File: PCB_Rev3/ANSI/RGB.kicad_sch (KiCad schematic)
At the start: 62 parts

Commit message: Wires optimization.
More GND hole still needed...
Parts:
- RGB1, RGB10, RGB11, RGB12, RGB13, RGB14, RGB15, RGB16, RGB17, RGB18, RGB19, RGB2, RGB20, RGB21, RGB22, RGB23, RGB24, RGB25, RGB26, RGB27, RGB28, RGB29, RGB3, RGB30, RGB31, RGB32, RGB33, RGB34, RGB35, RGB36, RGB37, RGB38, RGB39, RGB4, RGB40, RGB41, RGB42, RGB43, RGB44, RGB45, RGB46, RGB47, RGB48, RGB49, RGB5, RGB50, RGB51, RGB52, RGB53, RGB54, RGB55, RGB56, RGB57, RGB58, RGB59, RGB6, RGB60, RGB61, RGB62, RGB7, RGB8, RGB9: footprint RGB:ws2812B_6028 -> PH60:WS2812B_Reverse
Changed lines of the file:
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@@
 			)
 		)
-		(property "Footprint" "RGB:ws2812B_6028"
+		(property "Footprint" "PH60:WS2812B_Reverse"
 			(at 185.42 64.77 0)
 			(effects
@@
 			)
 		)
-		(property "Footprint" "RGB:ws2812B_6028"
+		(property "Footprint" "PH60:WS2812B_Reverse"
 			(at 43.18 85.09 0)
 			(effects
@@
 			)
 		)
-		(property "Footprint" "RGB:ws2812B_6028"
+		(property "Footprint" "PH60:WS2812B_Reverse"
 			(at 185.42 105.41 0)
 			(effects
@@
 			)
 		)
-		(property "Footprint" "RGB:ws2812B_6028"
+		(property "Footprint" "PH60:WS2812B_Reverse"
 			(at 398.78 105.41 0)
 			(effects
@@
 			)
 		)
-		(property "Footprint" "RGB:ws2812B_6028"
+		(property "Footprint" "PH60:WS2812B_Reverse"
 			(at 78.74 105.41 0)
 			(effects
@@
 			)
 		)
-		(property "Footprint" "RGB:ws2812B_6028"
+		(property "Footprint" "PH60:WS2812B_Reverse"
 			(at 363.22 105.41 0)
 			(effects
@@
 			)
 		)
-		(property "Footprint" "RGB:ws2812B_6028"
+		(property "Footprint" "PH60:WS2812B_Reverse"
 			(at 469.9 64.77 0)
 			(effects
@@
 			)
 		)
-		(property "Footprint" "RGB:ws2812B_6028"
+		(property "Footprint" "PH60:WS2812B_Reverse"
 			(at 185.42 125.73 0)
 			(effects
@@
 			)
 		)
-		(property "Footprint" "RGB:ws2812B_6028"
+		(property "Footprint" "PH60:WS2812B_Reverse"
 			(at 220.98 85.09 0)
 			(effects
@@
 			)
 		)
-		(property "Footprint" "RGB:ws2812B_6028"
+		(property "Footprint" "PH60:WS2812B_Reverse"
 			(at 43.18 125.73 0)
 			(effects
@@
 			)
 		)
-		(property "Footprint" "RGB:ws2812B_6028"
+		(property "Footprint" "PH60:WS2812B_Reverse"
 			(at 327.66 44.45 0)
 			(effects
@@
 			)
 		)
-		(property "Footprint" "RGB:ws2812B_6028"
+		(property "Footprint" "PH60:WS2812B_Reverse"
 			(at 434.34 44.45 0)
 			(effects
@@
 			)
 		)
-		(property "Footprint" "RGB:ws2812B_6028"
+		(property "Footprint" "PH60:WS2812B_Reverse"
 			(at 256.54 44.45 0)
 			(effects
@@
 			)
 		)
-		(property "Footprint" "RGB:ws2812B_6028"
+		(property "Footprint" "PH60:WS2812B_Reverse"
 			(at 505.46 44.45 0)
 			(effects
@@
 			)
 		)
-		(property "Footprint" "RGB:ws2812B_6028"
+		(property "Footprint" "PH60:WS2812B_Reverse"
 			(at 363.22 64.77 0)
 			(effects
@@
 			)
 		)
-		(property "Footprint" "RGB:ws2812B_6028"
+		(property "Footprint" "PH60:WS2812B_Reverse"
 			(at 185.42 44.45 0)
 			(effects
@@
 			)
 		)
-		(property "Footprint" "RGB:ws2812B_6028"
+		(property "Footprint" "PH60:WS2812B_Reverse"
 			(at 469.9 85.09 0)
 			(effects
@@
 			)
 		)
-		(property "Footprint" "RGB:ws2812B_6028"
+		(property "Footprint" "PH60:WS2812B_Reverse"
 			(at 256.54 64.77 0)
 			(effects
@@
 			)
 		)
-		(property "Footprint" "RGB:ws2812B_6028"
+		(property "Footprint" "PH60:WS2812B_Reverse"
 			(at 149.86 64.77 0)
 			(effects
@@
 			)
 		)
-		(property "Footprint" "RGB:ws2812B_6028"
+		(property "Footprint" "PH60:WS2812B_Reverse"
 			(at 434.34 64.77 0)
 			(effects
@@
 			)
 		)
-		(property "Footprint" "RGB:ws2812B_6028"
+		(property "Footprint" "PH60:WS2812B_Reverse"
 			(at 114.3 64.77 0)
 			(effects
@@
 			)
 		)
-		(property "Footprint" "RGB:ws2812B_6028"
+		(property "Footprint" "PH60:WS2812B_Reverse"
 			(at 292.1 44.45 0)
 			(effects
@@
 			)
 		)
-		(property "Footprint" "RGB:ws2812B_6028"
+		(property "Footprint" "PH60:WS2812B_Reverse"
 			(at 78.74 64.77 0)
 			(effects
@@
 			)
 		)
-		(property "Footprint" "RGB:ws2812B_6028"
+		(property "Footprint" "PH60:WS2812B_Reverse"
 			(at 43.18 105.41 0)
 			(effects
@@
 			)
 		)
-		(property "Footprint" "RGB:ws2812B_6028"
+		(property "Footprint" "PH60:WS2812B_Reverse"
 			(at 78.74 85.09 0)
 			(effects
@@
 			)
 		)
-		(property "Footprint" "RGB:ws2812B_6028"
+		(property "Footprint" "PH60:WS2812B_Reverse"
 			(at 43.18 64.77 0)
 			(effects
@@
 			)
 		)
-		(property "Footprint" "RGB:ws2812B_6028"
+		(property "Footprint" "PH60:WS2812B_Reverse"
 			(at 363.22 44.45 0)
 			(effects
@@
 			)
 		)
-		(property "Footprint" "RGB:ws2812B_6028"
+		(property "Footprint" "PH60:WS2812B_Reverse"
 			(at 220.98 44.45 0)
 			(effects
@@
 			)
 		)
-		(property "Footprint" "RGB:ws2812B_6028"
+		(property "Footprint" "PH60:WS2812B_Reverse"
 			(at 469.9 44.45 0)
 			(effects
@@
 			)
 		)
-		(property "Footprint" "RGB:ws2812B_6028"
+		(property "Footprint" "PH60:WS2812B_Reverse"
 			(at 292.1 85.09 0)
 			(effects
@@
 			)
 		)
-		(property "Footprint" "RGB:ws2812B_6028"
+		(property "Footprint" "PH60:WS2812B_Reverse"
 			(at 114.3 44.45 0)
 			(effects
@@
 			)
 		)
-		(property "Footprint" "RGB:ws2812B_6028"
+		(property "Footprint" "PH60:WS2812B_Reverse"
 			(at 78.74 125.73 0)
 			(effects
@@
 			)
 		)
-		(property "Footprint" "RGB:ws2812B_6028"
+		(property "Footprint" "PH60:WS2812B_Reverse"
 			(at 220.98 64.77 0)
 			(effects
@@
 			)
 		)
-		(property "Footprint" "RGB:ws2812B_6028"
+		(property "Footprint" "PH60:WS2812B_Reverse"
 			(at 398.78 44.45 0)
 			(effects
@@
 			)
 		)
-		(property "Footprint" "RGB:ws2812B_6028"
+		(property "Footprint" "PH60:WS2812B_Reverse"
 			(at 398.78 64.77 0)
 			(effects
@@
 			)
 		)
-		(property "Footprint" "RGB:ws2812B_6028"
+		(property "Footprint" "PH60:WS2812B_Reverse"
 			(at 114.3 105.41 0)
 			(effects
@@
 			)
 		)
-		(property "Footprint" "RGB:ws2812B_6028"
+		(property "Footprint" "PH60:WS2812B_Reverse"
 			(at 43.18 44.45 0)
 			(effects
@@
 			)
 		)
-		(property "Footprint" "RGB:ws2812B_6028"
+		(property "Footprint" "PH60:WS2812B_Reverse"
 			(at 505.46 64.77 0)
 			(effects
@@
 			)
 		)
-		(property "Footprint" "RGB:ws2812B_6028"
+		(property "Footprint" "PH60:WS2812B_Reverse"
 			(at 149.86 105.41 0)
 			(effects
@@
 			)
 		)
-		(property "Footprint" "RGB:ws2812B_6028"
+		(property "Footprint" "PH60:WS2812B_Reverse"
 			(at 292.1 64.77 0)
 			(effects
@@
 			)
 		)
-		(property "Footprint" "RGB:ws2812B_6028"
+		(property "Footprint" "PH60:WS2812B_Reverse"
 			(at 78.74 44.45 0)
 			(effects
@@
 			)
 		)
-		(property "Footprint" "RGB:ws2812B_6028"
+		(property "Footprint" "PH60:WS2812B_Reverse"
 			(at 256.54 85.09 0)
 			(effects
@@
 			)
 		)
-		(property "Footprint" "RGB:ws2812B_6028"
+		(property "Footprint" "PH60:WS2812B_Reverse"
 			(at 114.3 85.09 0)
 			(effects
@@
 			)
 		)
-		(property "Footprint" "RGB:ws2812B_6028"
+		(property "Footprint" "PH60:WS2812B_Reverse"
 			(at 363.22 85.09 0)
 			(effects
@@
 			)
 		)
-		(property "Footprint" "RGB:ws2812B_6028"
+		(property "Footprint" "PH60:WS2812B_Reverse"
 			(at 469.9 105.41 0)
 			(effects
@@
 			)
 		)
-		(property "Footprint" "RGB:ws2812B_6028"
+		(property "Footprint" "PH60:WS2812B_Reverse"
 			(at 114.3 125.73 0)
 			(effects
@@
 			)
 		)
-		(property "Footprint" "RGB:ws2812B_6028"
+		(property "Footprint" "PH60:WS2812B_Reverse"
 			(at 327.66 85.09 0)
 			(effects
@@
 			)
 		)
-		(property "Footprint" "RGB:ws2812B_6028"
+		(property "Footprint" "PH60:WS2812B_Reverse"
 			(at 434.34 105.41 0)
 			(effects
@@
 			)
 		)
-		(property "Footprint" "RGB:ws2812B_6028"
+		(property "Footprint" "PH60:WS2812B_Reverse"
 			(at 327.66 105.41 0)
 			(effects
@@
 			)
 		)
-		(property "Footprint" "RGB:ws2812B_6028"
+		(property "Footprint" "PH60:WS2812B_Reverse"
 			(at 256.54 105.41 0)
 			(effects
@@
 			)
 		)
-		(property "Footprint" "RGB:ws2812B_6028"
+		(property "Footprint" "PH60:WS2812B_Reverse"
 			(at 398.78 85.09 0)
 			(effects
@@
 			)
 		)
-		(property "Footprint" "RGB:ws2812B_6028"
+		(property "Footprint" "PH60:WS2812B_Reverse"
 			(at 292.1 105.41 0)
 			(effects
@@
 			)
 		)
-		(property "Footprint" "RGB:ws2812B_6028"
+		(property "Footprint" "PH60:WS2812B_Reverse"
 			(at 149.86 125.73 0)
 			(effects
@@
 			)
 		)
-		(property "Footprint" "RGB:ws2812B_6028"
+		(property "Footprint" "PH60:WS2812B_Reverse"
 			(at 220.98 105.41 0)
 			(effects
@@
 			)
 		)
-		(property "Footprint" "RGB:ws2812B_6028"
+		(property "Footprint" "PH60:WS2812B_Reverse"
 			(at 149.86 44.45 0)
 			(effects
@@
 			)
 		)
-		(property "Footprint" "RGB:ws2812B_6028"
+		(property "Footprint" "PH60:WS2812B_Reverse"
 			(at 434.34 85.09 0)
 			(effects
@@
 			)
 		)
-		(property "Footprint" "RGB:ws2812B_6028"
+		(property "Footprint" "PH60:WS2812B_Reverse"
 			(at 149.86 85.09 0)
 			(effects
@@
 			)
 		)
-		(property "Footprint" "RGB:ws2812B_6028"
+		(property "Footprint" "PH60:WS2812B_Reverse"
 			(at 327.66 64.77 0)
 			(effects
@@
 			)
 		)
-		(property "Footprint" "RGB:ws2812B_6028"
+		(property "Footprint" "PH60:WS2812B_Reverse"
 			(at 185.42 85.09 0)
 			(effects
@@
 			)
 		)
-		(property "Footprint" "RGB:ws2812B_6028"
+		(property "Footprint" "PH60:WS2812B_Reverse"
 			(at 220.98 125.73 0)
 			(effects
@@
 			)
 		)
-		(property "Footprint" "RGB:ws2812B_6028"
+		(property "Footprint" "PH60:WS2812B_Reverse"
 			(at 505.46 85.09 0)
 			(effects
@@
 			)
 		)
-		(property "Footprint" "RGB:ws2812B_6028"
+		(property "Footprint" "PH60:WS2812B_Reverse"
 			(at 505.46 105.41 0)
 			(effects

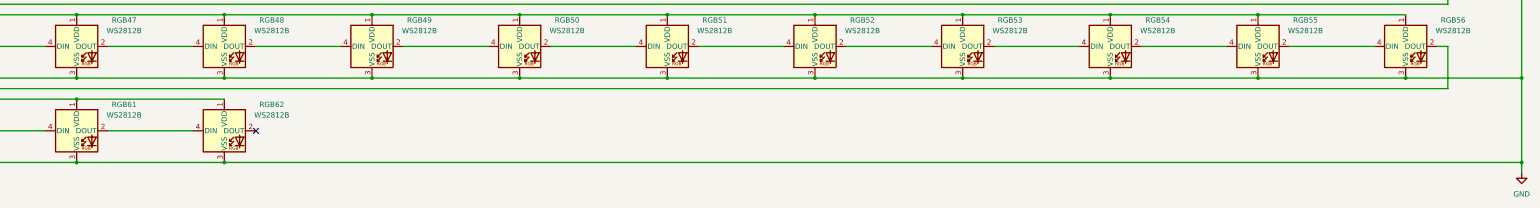
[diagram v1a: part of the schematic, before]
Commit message: Better wiring.
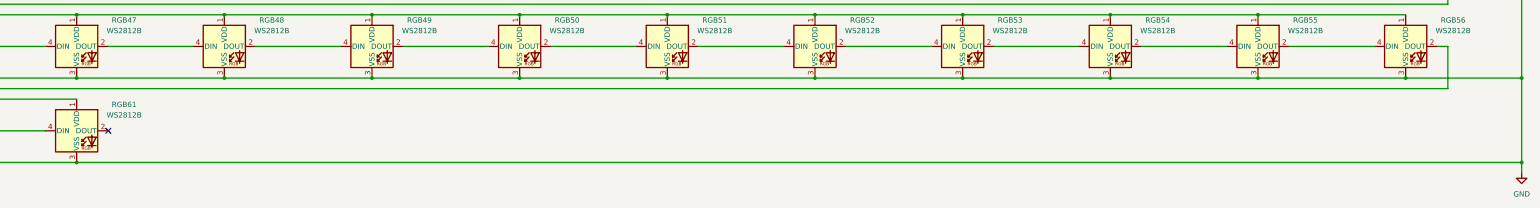
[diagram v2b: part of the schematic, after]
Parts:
- removed RGB62: WS2812B, PH60:WS2812B_Reverse, symbol LED:WS2812B
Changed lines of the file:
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@@
 	)
 	(junction
-		(at 184.15 110.49)
-		(diameter 0)
-		(color 0 0 0 0)
-	)
-	(junction
 		(at 255.27 105.41)
 		(diameter 0)
@@
 	)
 	(junction
-		(at 219.71 125.73)
-		(diameter 0)
-		(color 0 0 0 0)
-	)
-	(junction
 		(at 148.59 49.53)
 		(diameter 0)
@@
 	)
 	(no_connect
-		(at 227.33 118.11)
+		(at 191.77 118.11)
 	)
 	(wire
@@
 	(wire
 		(pts
-			(xy 219.71 125.73) (xy 532.13 125.73)
-		)
-		(stroke
-			(width 0)
-			(type default)
-		)
-	)
-	(wire
-		(pts
 			(xy 49.53 97.79) (xy 69.85 97.79)
 		)
@@
 	(wire
 		(pts
-			(xy 184.15 125.73) (xy 219.71 125.73)
+			(xy 433.07 90.17) (xy 468.63 90.17)
 		)
 		(stroke
@@
 	(wire
 		(pts
-			(xy 433.07 90.17) (xy 468.63 90.17)
+			(xy 504.19 29.21) (xy 520.7 29.21)
 		)
 		(stroke
@@
 	(wire
 		(pts
-			(xy 504.19 29.21) (xy 520.7 29.21)
+			(xy 184.15 125.73) (xy 532.13 125.73)
 		)
 		(stroke
@@
 	(wire
 		(pts
-			(xy 191.77 118.11) (xy 212.09 118.11)
-		)
-		(stroke
-			(width 0)
-			(type default)
-		)
-	)
-	(wire
-		(pts
 			(xy 120.65 118.11) (xy 140.97 118.11)
 		)
@@
 	(wire
 		(pts
-			(xy 184.15 110.49) (xy 219.71 110.49)
-		)
-		(stroke
-			(width 0)
-			(type default)
-		)
-	)
-	(wire
-		(pts
 			(xy 77.47 64.77) (xy 113.03 64.77)
 		)
@@
 					(unit 1)
 				)
-			)
-		)
-	)
-	(symbol
-		(lib_id "LED:WS2812B")
-		(at 219.71 118.11 0)
-		(unit 1)
-		(exclude_from_sim no)
-		(in_bom yes)
-		(on_board yes)
-		(dnp no)
-		(fields_autoplaced yes)
-		(property "Reference" "RGB62"
-			(at 231.14 111.7914 0)
-			(effects
-				(font
-					(size 1.27 1.27)
-				)
-			)
-		)
-		(property "Value" "WS2812B"
-			(at 231.14 114.3314 0)
-			(effects
-				(font
-					(size 1.27 1.27)
-				)
-			)
-		)
-		(property "Footprint" "PH60:WS2812B_Reverse"
-			(at 220.98 125.73 0)
-			(effects
-				(font
-					(size 1.27 1.27)
-				)
-				(justify left top)
-				(hide yes)
-			)
-		)
-		(property "Datasheet" "https://cdn-shop.adafruit.com/datasheets/WS2812B.pdf"
-			(at 222.25 127.635 0)
-			(effects
-				(font
-					(size 1.27 1.27)
-				)
-				(justify left top)
-				(hide yes)
-			)
-		)
-		(property "Description" "RGB LED with integrated controller"
-			(at 219.71 118.11 0)
-			(effects
-				(font
-					(size 1.27 1.27)
-				)
-				(hide yes)
-			)
-		)
-		(pin "4"
-		)
-		(pin "3"
-		)
-		(pin "2"
-		)
-		(pin "1"
-		)
-		(instances
-			(project "PH60_Rev3"
-				(path "/dca0f898-8fdb-4522-a51d-f4f4238906e7/c0337f82-e68f-485d-b406-18ae8e593971"
-					(reference "RGB62")
-					(unit 1)
-				)

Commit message: Finish board design
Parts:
- RGB1, RGB10, RGB11, RGB12, RGB13, RGB14, RGB15, RGB16, RGB17, RGB18, RGB19, RGB2, RGB20, RGB21, RGB22, RGB23, RGB24, RGB25, RGB26, RGB27, RGB28, RGB29, RGB3, RGB30, RGB31, RGB32, RGB33, RGB34, RGB35, RGB36, RGB37, RGB38, RGB39, RGB4, RGB40, RGB41, RGB42, RGB43, RGB44, RGB45, RGB46, RGB47, RGB48, RGB49, RGB5, RGB50, RGB51, RGB52, RGB53, RGB54, RGB55, RGB56, RGB57, RGB58, RGB59, RGB6, RGB60, RGB61, RGB7, RGB8, RGB9: footprint PH60:WS2812B_Reverse -> PH60:ws2812b_6028
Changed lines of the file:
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@@
 			)
 		)
-		(property "Footprint" "PH60:WS2812B_Reverse"
+		(property "Footprint" "PH60:ws2812b_6028"
 			(at 185.42 64.77 0)
 			(effects
@@
 			)
 		)
-		(property "Footprint" "PH60:WS2812B_Reverse"
+		(property "Footprint" "PH60:ws2812b_6028"
 			(at 43.18 85.09 0)
 			(effects
@@
 			)
 		)
-		(property "Footprint" "PH60:WS2812B_Reverse"
+		(property "Footprint" "PH60:ws2812b_6028"
 			(at 185.42 105.41 0)
 			(effects
@@
 			)
 		)
-		(property "Footprint" "PH60:WS2812B_Reverse"
+		(property "Footprint" "PH60:ws2812b_6028"
 			(at 398.78 105.41 0)
 			(effects
@@
 			)
 		)
-		(property "Footprint" "PH60:WS2812B_Reverse"
+		(property "Footprint" "PH60:ws2812b_6028"
 			(at 78.74 105.41 0)
 			(effects
@@
 			)
 		)
-		(property "Footprint" "PH60:WS2812B_Reverse"
+		(property "Footprint" "PH60:ws2812b_6028"
 			(at 363.22 105.41 0)
 			(effects
@@
 			)
 		)
-		(property "Footprint" "PH60:WS2812B_Reverse"
+		(property "Footprint" "PH60:ws2812b_6028"
 			(at 469.9 64.77 0)
 			(effects
@@
 			)
 		)
-		(property "Footprint" "PH60:WS2812B_Reverse"
+		(property "Footprint" "PH60:ws2812b_6028"
 			(at 185.42 125.73 0)
 			(effects
@@
 			)
 		)
-		(property "Footprint" "PH60:WS2812B_Reverse"
+		(property "Footprint" "PH60:ws2812b_6028"
 			(at 220.98 85.09 0)
 			(effects
@@
 			)
 		)
-		(property "Footprint" "PH60:WS2812B_Reverse"
+		(property "Footprint" "PH60:ws2812b_6028"
 			(at 43.18 125.73 0)
 			(effects
@@
 			)
 		)
-		(property "Footprint" "PH60:WS2812B_Reverse"
+		(property "Footprint" "PH60:ws2812b_6028"
 			(at 327.66 44.45 0)
 			(effects
@@
 			)
 		)
-		(property "Footprint" "PH60:WS2812B_Reverse"
+		(property "Footprint" "PH60:ws2812b_6028"
 			(at 434.34 44.45 0)
 			(effects
@@
 			)
 		)
-		(property "Footprint" "PH60:WS2812B_Reverse"
+		(property "Footprint" "PH60:ws2812b_6028"
 			(at 256.54 44.45 0)
 			(effects
@@
 			)
 		)
-		(property "Footprint" "PH60:WS2812B_Reverse"
+		(property "Footprint" "PH60:ws2812b_6028"
 			(at 505.46 44.45 0)
 			(effects
@@
 			)
 		)
-		(property "Footprint" "PH60:WS2812B_Reverse"
+		(property "Footprint" "PH60:ws2812b_6028"
 			(at 363.22 64.77 0)
 			(effects
@@
 			)
 		)
-		(property "Footprint" "PH60:WS2812B_Reverse"
+		(property "Footprint" "PH60:ws2812b_6028"
 			(at 185.42 44.45 0)
 			(effects
@@
 			)
 		)
-		(property "Footprint" "PH60:WS2812B_Reverse"
+		(property "Footprint" "PH60:ws2812b_6028"
 			(at 469.9 85.09 0)
 			(effects
@@
 			)
 		)
-		(property "Footprint" "PH60:WS2812B_Reverse"
+		(property "Footprint" "PH60:ws2812b_6028"
 			(at 256.54 64.77 0)
 			(effects
@@
 			)
 		)
-		(property "Footprint" "PH60:WS2812B_Reverse"
+		(property "Footprint" "PH60:ws2812b_6028"
 			(at 149.86 64.77 0)
 			(effects
@@
 			)
 		)
-		(property "Footprint" "PH60:WS2812B_Reverse"
+		(property "Footprint" "PH60:ws2812b_6028"
 			(at 434.34 64.77 0)
 			(effects
@@
 			)
 		)
-		(property "Footprint" "PH60:WS2812B_Reverse"
+		(property "Footprint" "PH60:ws2812b_6028"
 			(at 114.3 64.77 0)
 			(effects
@@
 			)
 		)
-		(property "Footprint" "PH60:WS2812B_Reverse"
+		(property "Footprint" "PH60:ws2812b_6028"
 			(at 292.1 44.45 0)
 			(effects
@@
 			)
 		)
-		(property "Footprint" "PH60:WS2812B_Reverse"
+		(property "Footprint" "PH60:ws2812b_6028"
 			(at 78.74 64.77 0)
 			(effects
@@
 			)
 		)
-		(property "Footprint" "PH60:WS2812B_Reverse"
+		(property "Footprint" "PH60:ws2812b_6028"
 			(at 43.18 105.41 0)
 			(effects
@@
 			)
 		)
-		(property "Footprint" "PH60:WS2812B_Reverse"
+		(property "Footprint" "PH60:ws2812b_6028"
 			(at 78.74 85.09 0)
 			(effects
@@
 			)
 		)
-		(property "Footprint" "PH60:WS2812B_Reverse"
+		(property "Footprint" "PH60:ws2812b_6028"
 			(at 43.18 64.77 0)
 			(effects
@@
 			)
 		)
-		(property "Footprint" "PH60:WS2812B_Reverse"
+		(property "Footprint" "PH60:ws2812b_6028"
 			(at 363.22 44.45 0)
 			(effects
@@
 			)
 		)
-		(property "Footprint" "PH60:WS2812B_Reverse"
+		(property "Footprint" "PH60:ws2812b_6028"
 			(at 220.98 44.45 0)
 			(effects
@@
 			)
 		)
-		(property "Footprint" "PH60:WS2812B_Reverse"
+		(property "Footprint" "PH60:ws2812b_6028"
 			(at 469.9 44.45 0)
 			(effects
@@
 			)
 		)
-		(property "Footprint" "PH60:WS2812B_Reverse"
+		(property "Footprint" "PH60:ws2812b_6028"
 			(at 292.1 85.09 0)
 			(effects
@@
 			)
 		)
-		(property "Footprint" "PH60:WS2812B_Reverse"
+		(property "Footprint" "PH60:ws2812b_6028"
 			(at 114.3 44.45 0)
 			(effects
@@
 			)
 		)
-		(property "Footprint" "PH60:WS2812B_Reverse"
+		(property "Footprint" "PH60:ws2812b_6028"
 			(at 78.74 125.73 0)
 			(effects
@@
 			)
 		)
-		(property "Footprint" "PH60:WS2812B_Reverse"
+		(property "Footprint" "PH60:ws2812b_6028"
 			(at 220.98 64.77 0)
 			(effects
@@
 			)
 		)
-		(property "Footprint" "PH60:WS2812B_Reverse"
+		(property "Footprint" "PH60:ws2812b_6028"
 			(at 398.78 44.45 0)
 			(effects
@@
 			)
 		)
-		(property "Footprint" "PH60:WS2812B_Reverse"
+		(property "Footprint" "PH60:ws2812b_6028"
 			(at 398.78 64.77 0)
 			(effects
@@
 			)
 		)
-		(property "Footprint" "PH60:WS2812B_Reverse"
+		(property "Footprint" "PH60:ws2812b_6028"
 			(at 114.3 105.41 0)
 			(effects
@@
 			)
 		)
-		(property "Footprint" "PH60:WS2812B_Reverse"
+		(property "Footprint" "PH60:ws2812b_6028"
 			(at 43.18 44.45 0)
 			(effects
@@
 			)
 		)
-		(property "Footprint" "PH60:WS2812B_Reverse"
+		(property "Footprint" "PH60:ws2812b_6028"
 			(at 505.46 64.77 0)
 			(effects
@@
 			)
 		)
-		(property "Footprint" "PH60:WS2812B_Reverse"
+		(property "Footprint" "PH60:ws2812b_6028"
 			(at 149.86 105.41 0)
 			(effects
@@
 			)
 		)
-		(property "Footprint" "PH60:WS2812B_Reverse"
+		(property "Footprint" "PH60:ws2812b_6028"
 			(at 292.1 64.77 0)
 			(effects
@@
 			)
 		)
-		(property "Footprint" "PH60:WS2812B_Reverse"
+		(property "Footprint" "PH60:ws2812b_6028"
 			(at 78.74 44.45 0)
 			(effects
@@
 		(dnp no)
 		(fields_autoplaced yes)
-		(property "Reference" "#PWR025"
+		(property "Reference" "#PWR036"
 			(at 532.13 134.62 0)
 			(effects
@@
 			(project ""
 				(path "/dca0f898-8fdb-4522-a51d-f4f4238906e7/c0337f82-e68f-485d-b406-18ae8e593971"
-					(reference "#PWR025")
+					(reference "#PWR036")
 					(unit 1)
 				)
@@
 			)
 		)
-		(property "Footprint" "PH60:WS2812B_Reverse"
+		(property "Footprint" "PH60:ws2812b_6028"
 			(at 256.54 85.09 0)
 			(effects
@@
 			)
 		)
-		(property "Footprint" "PH60:WS2812B_Reverse"
+		(property "Footprint" "PH60:ws2812b_6028"
 			(at 114.3 85.09 0)
 			(effects
@@
 			)
 		)
-		(property "Footprint" "PH60:WS2812B_Reverse"
+		(property "Footprint" "PH60:ws2812b_6028"
 			(at 363.22 85.09 0)
 			(effects
@@
 			)
 		)
-		(property "Footprint" "PH60:WS2812B_Reverse"
+		(property "Footprint" "PH60:ws2812b_6028"
 			(at 469.9 105.41 0)
 			(effects
@@
 			)
 		)
-		(property "Footprint" "PH60:WS2812B_Reverse"
+		(property "Footprint" "PH60:ws2812b_6028"
 			(at 114.3 125.73 0)
 			(effects
@@
 			)
 		)
-		(property "Footprint" "PH60:WS2812B_Reverse"
+		(property "Footprint" "PH60:ws2812b_6028"
 			(at 327.66 85.09 0)
 			(effects
@@
 			)
 		)
-		(property "Footprint" "PH60:WS2812B_Reverse"
+		(property "Footprint" "PH60:ws2812b_6028"
 			(at 434.34 105.41 0)
 			(effects
@@
 			)
 		)
-		(property "Footprint" "PH60:WS2812B_Reverse"
+		(property "Footprint" "PH60:ws2812b_6028"
 			(at 327.66 105.41 0)
 			(effects
@@
 			)
 		)
-		(property "Footprint" "PH60:WS2812B_Reverse"
+		(property "Footprint" "PH60:ws2812b_6028"
 			(at 256.54 105.41 0)
 			(effects
@@
 			)
 		)
-		(property "Footprint" "PH60:WS2812B_Reverse"
+		(property "Footprint" "PH60:ws2812b_6028"
 			(at 398.78 85.09 0)
 			(effects
@@
 		(dnp no)
 		(fields_autoplaced yes)
-		(property "Reference" "#PWR024"
+		(property "Reference" "#PWR035"
 			(at 29.21 124.46 0)
 			(effects
@@
 			(project ""
 				(path "/dca0f898-8fdb-4522-a51d-f4f4238906e7/c0337f82-e68f-485d-b406-18ae8e593971"
-					(reference "#PWR024")
+					(reference "#PWR035")
 					(unit 1)
 				)
@@
 			)
 		)
-		(property "Footprint" "PH60:WS2812B_Reverse"
+		(property "Footprint" "PH60:ws2812b_6028"
 			(at 292.1 105.41 0)
 			(effects
@@
 			)
 		)
-		(property "Footprint" "PH60:WS2812B_Reverse"
+		(property "Footprint" "PH60:ws2812b_6028"
 			(at 149.86 125.73 0)
 			(effects
@@
 			)
 		)
-		(property "Footprint" "PH60:WS2812B_Reverse"
+		(property "Footprint" "PH60:ws2812b_6028"
 			(at 220.98 105.41 0)
 			(effects
@@
 			)
 		)
-		(property "Footprint" "PH60:WS2812B_Reverse"
+		(property "Footprint" "PH60:ws2812b_6028"
 			(at 149.86 44.45 0)
 			(effects
@@
 			)
 		)
-		(property "Footprint" "PH60:WS2812B_Reverse"
+		(property "Footprint" "PH60:ws2812b_6028"
 			(at 434.34 85.09 0)
 			(effects
@@
 			)
 		)
-		(property "Footprint" "PH60:WS2812B_Reverse"
+		(property "Footprint" "PH60:ws2812b_6028"
 			(at 149.86 85.09 0)
 			(effects
@@
 			)
 		)
-		(property "Footprint" "PH60:WS2812B_Reverse"
+		(property "Footprint" "PH60:ws2812b_6028"
 			(at 327.66 64.77 0)
 			(effects
@@
 			)
 		)
-		(property "Footprint" "PH60:WS2812B_Reverse"
+		(property "Footprint" "PH60:ws2812b_6028"
 			(at 185.42 85.09 0)
 			(effects
@@
 			)
 		)
-		(property "Footprint" "PH60:WS2812B_Reverse"
+		(property "Footprint" "PH60:ws2812b_6028"
 			(at 505.46 85.09 0)
 			(effects
@@
 			)
 		)
-		(property "Footprint" "PH60:WS2812B_Reverse"
+		(property "Footprint" "PH60:ws2812b_6028"
 			(at 505.46 105.41 0)
 			(effects
